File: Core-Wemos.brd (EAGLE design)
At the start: 86.5 x 100 mm, 51 parts, among them J2 CONNECTOR-GROVE-4P-2.0-347013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, J3 IO4

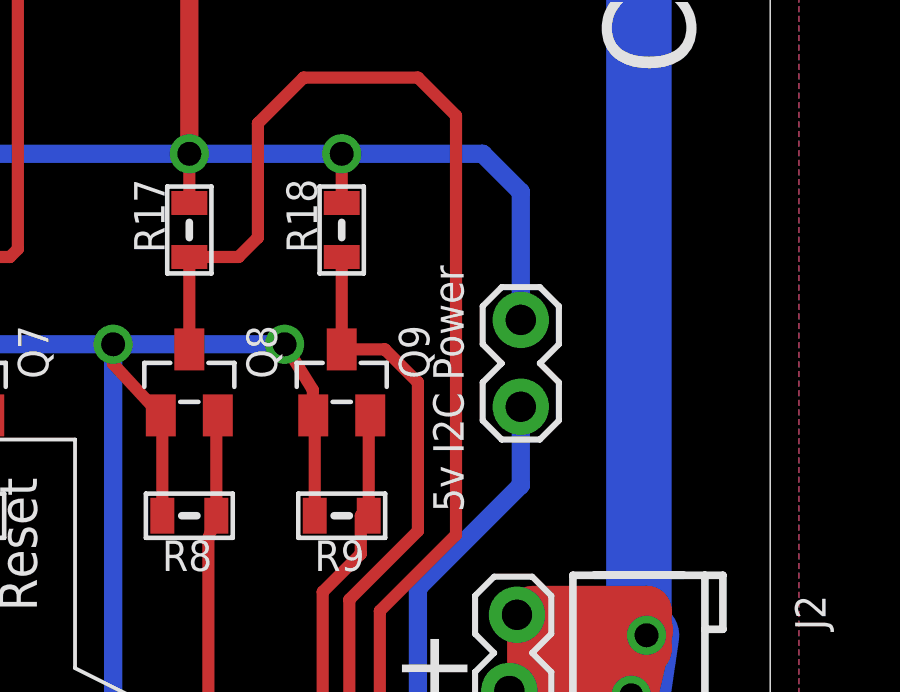
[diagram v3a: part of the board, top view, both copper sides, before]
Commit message: added missing component values
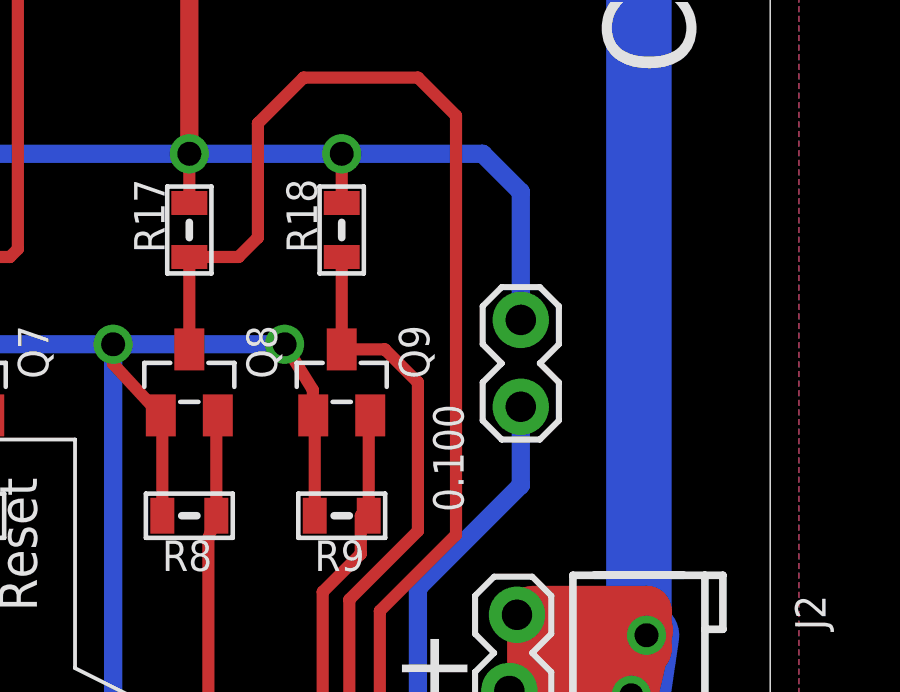
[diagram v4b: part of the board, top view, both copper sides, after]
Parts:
- CMRI-IO: value (none) -> 0.100; device SPCoast:CON-CMRI-IO -> SPCoast:1X05-CMRI-IO
- I2C-OLED: value (none) -> OLED
- JP1: value 5v I2C Power -> 0.100
- Q1, Q2, Q3, Q4, Q5, Q6, Q7, Q8, Q9: value (none) -> BSS138
- VR5.0: value 5v -> cj7805
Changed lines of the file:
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@@
 <attribute name="VALUE" x="66.04" y="74.295" size="1.27" layer="27" font="vector" rot="R180"/>
 </element>
-<element name="JP1" library="SparkFun-Connectors" package="1X02_LOCK" value="5v I2C Power" x="72.009" y="48.895" smashed="yes" rot="R90">
+<element name="JP1" library="SparkFun-Connectors" package="1X02_LOCK" value="0.100" x="72.009" y="48.895" smashed="yes" rot="R90">
 <attribute name="VALUE" x="70.104" y="45.212" size="1.016" layer="21" rot="R90"/>
 </element>
@@
 <attribute name="VALUE" x="16.79575" y="62.4205" size="1.016" layer="27" rot="R90"/>
 </element>
-<element name="VR5.0" library="SPCoast" package="TO-252" value="5v" x="20.32" y="73.66" smashed="yes" rot="R90">
+<element name="VR5.0" library="SPCoast" package="TO-252" value="cj7805" x="20.32" y="73.66" smashed="yes" rot="R90">
 <attribute name="NAME" x="21.43125" y="75.40625" size="1.016" layer="25" ratio="11" rot="R270"/>
 <attribute name="VALUE" x="21.7805" y="69.723" size="1.27" layer="27" ratio="10" rot="R180"/>
@@
 <attribute name="VALUE" x="5.08" y="67.31" size="1.27" layer="27"/>
 </element>
-<element name="Q7" library="SPCoast" package="SOT23" value="" x="53.34" y="49.53" smashed="yes" rot="R270">
+<element name="Q7" library="SPCoast" package="SOT23" value="BSS138" x="53.34" y="49.53" smashed="yes" rot="R270">
 <attribute name="NAME" x="55.245" y="51.435" size="1.016" layer="25" rot="R270"/>
 <attribute name="VALUE" x="50.165" y="51.435" size="1.27" layer="27" rot="R270"/>
@@
 <attribute name="VALUE" x="54.737" y="53.594" size="0.4064" layer="27" rot="R90"/>
 </element>
-<element name="Q8" library="SPCoast" package="SOT23" value="" x="60.96" y="49.53" smashed="yes" rot="R270">
+<element name="Q8" library="SPCoast" package="SOT23" value="BSS138" x="60.96" y="49.53" smashed="yes" rot="R270">
 <attribute name="NAME" x="62.865" y="51.435" size="1.016" layer="25" rot="R270"/>
 <attribute name="VALUE" x="57.785" y="51.435" size="1.27" layer="27" rot="R270"/>
@@
 <attribute name="VALUE" x="62.357" y="53.594" size="0.4064" layer="27" rot="R90"/>
 </element>
-<element name="Q9" library="SPCoast" package="SOT23" value="" x="66.04" y="49.53" smashed="yes" rot="R270">
+<element name="Q9" library="SPCoast" package="SOT23" value="BSS138" x="66.04" y="49.53" smashed="yes" rot="R270">
 <attribute name="NAME" x="67.945" y="51.435" size="1.016" layer="25" rot="R270"/>
 <attribute name="VALUE" x="62.865" y="51.435" size="1.27" layer="27" rot="R270"/>
@@
 <attribute name="VALUE" x="67.437" y="53.594" size="0.4064" layer="27" rot="R90"/>
 </element>
-<element name="Q1" library="SPCoast" package="SOT23" value="" x="21.59" y="49.53" smashed="yes" rot="R270">
+<element name="Q1" library="SPCoast" package="SOT23" value="BSS138" x="21.59" y="49.53" smashed="yes" rot="R270">
 <attribute name="NAME" x="23.495" y="51.435" size="1.016" layer="25" rot="R270"/>
 <attribute name="VALUE" x="18.415" y="51.435" size="1.27" layer="27" rot="R270"/>
@@
 <attribute name="VALUE" x="22.987" y="53.594" size="0.4064" layer="27" rot="R90"/>
 </element>
-<element name="Q2" library="SPCoast" package="SOT23" value="" x="26.67" y="49.53" smashed="yes" rot="R270">
+<element name="Q2" library="SPCoast" package="SOT23" value="BSS138" x="26.67" y="49.53" smashed="yes" rot="R270">
 <attribute name="NAME" x="28.575" y="51.435" size="1.016" layer="25" rot="R270"/>
 <attribute name="VALUE" x="23.495" y="51.435" size="1.27" layer="27" rot="R270"/>
@@
 <attribute name="VALUE" x="28.067" y="53.594" size="0.4064" layer="27" rot="R90"/>
 </element>
-<element name="Q3" library="SPCoast" package="SOT23" value="" x="31.75" y="49.53" smashed="yes" rot="R270">
+<element name="Q3" library="SPCoast" package="SOT23" value="BSS138" x="31.75" y="49.53" smashed="yes" rot="R270">
 <attribute name="NAME" x="33.655" y="51.435" size="1.016" layer="25" rot="R270"/>
 <attribute name="VALUE" x="28.575" y="51.435" size="1.27" layer="27" rot="R270"/>
@@
 <attribute name="VALUE" x="33.147" y="53.594" size="0.4064" layer="27" rot="R90"/>
 </element>
-<element name="Q4" library="SPCoast" package="SOT23" value="" x="40.005" y="49.53" smashed="yes" rot="R270">
+<element name="Q4" library="SPCoast" package="SOT23" value="BSS138" x="40.005" y="49.53" smashed="yes" rot="R270">
 <attribute name="NAME" x="41.91" y="51.435" size="1.016" layer="25" rot="R270"/>
 <attribute name="VALUE" x="36.83" y="51.435" size="1.27" layer="27" rot="R270"/>
@@
 <attribute name="VALUE" x="41.402" y="53.594" size="0.4064" layer="27" rot="R90"/>
 </element>
-<element name="Q5" library="SPCoast" package="SOT23" value="" x="44.45" y="49.53" smashed="yes" rot="R270">
+<element name="Q5" library="SPCoast" package="SOT23" value="BSS138" x="44.45" y="49.53" smashed="yes" rot="R270">
 <attribute name="NAME" x="46.355" y="51.435" size="1.016" layer="25" rot="R270"/>
 <attribute name="VALUE" x="41.275" y="51.435" size="1.27" layer="27" rot="R270"/>
@@
 <attribute name="VALUE" x="45.847" y="53.594" size="0.4064" layer="27" rot="R90"/>
 </element>
-<element name="Q6" library="SPCoast" package="SOT23" value="" x="48.895" y="49.53" smashed="yes" rot="R270">
+<element name="Q6" library="SPCoast" package="SOT23" value="BSS138" x="48.895" y="49.53" smashed="yes" rot="R270">
 <attribute name="NAME" x="50.8" y="51.435" size="1.016" layer="25" rot="R270"/>
 <attribute name="VALUE" x="45.72" y="51.435" size="1.27" layer="27" rot="R270"/>
@@
 <attribute name="VALUE" x="50.292" y="53.594" size="0.4064" layer="27" rot="R90"/>
 </element>
-<element name="CMRI-IO" library="SPCoast" package="CON-CMRI-IO" value="" x="6.35" y="31.75" smashed="yes" rot="R90">
+<element name="CMRI-IO" library="SPCoast" package="1X05-CMRI-IO" value="0.100" x="6.35" y="31.75" smashed="yes" rot="R90">
 <attribute name="NAME" x="6.8834" y="44.3992" size="1.016" layer="25" ratio="10" rot="R90"/>
 </element>
@@
 <attribute name="NAME" x="67.056" y="94.107" size="1.016" layer="25"/>
 </element>
-<element name="I2C-OLED" library="SPCoast" package="I2C-NOOUTLINE" value="" x="19.939" y="39.497" smashed="yes" rot="R180">
+<element name="I2C-OLED" library="SPCoast" package="I2C-NOOUTLINE" value="OLED" x="19.939" y="39.497" smashed="yes" rot="R180">
 <attribute name="NAME" x="16.637" y="43.307" size="1.016" layer="25" font="vector" ratio="11"/>
 <attribute name="VALUE" x="13.081" y="39.878" size="0.635" layer="27" font="vector" ratio="10" rot="R270"/>

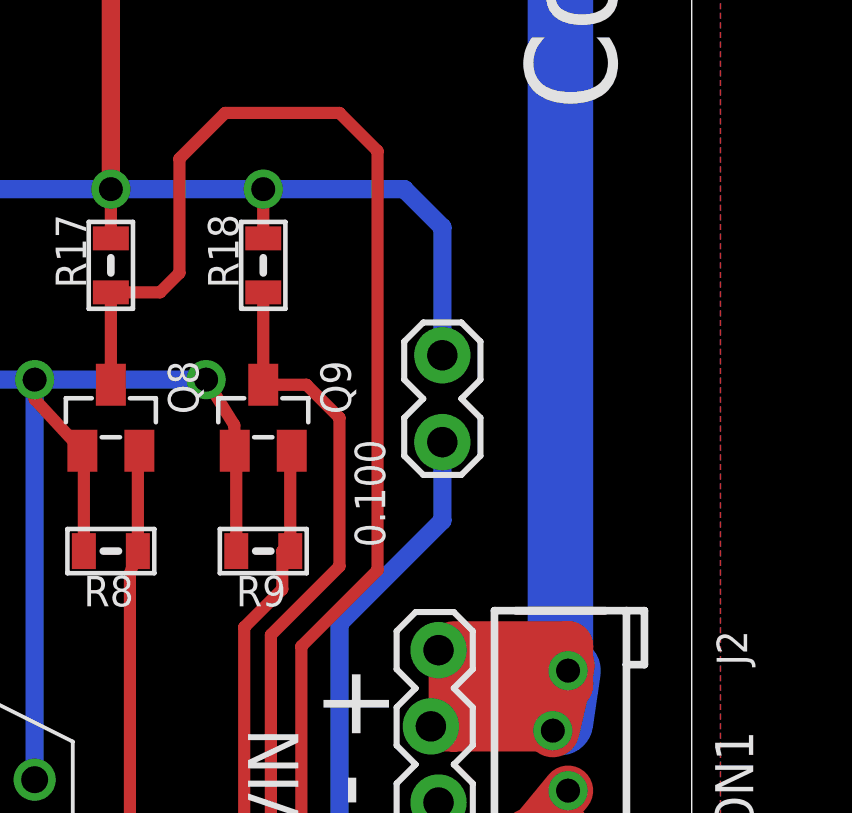
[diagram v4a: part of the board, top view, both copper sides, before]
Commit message: updated part names and values
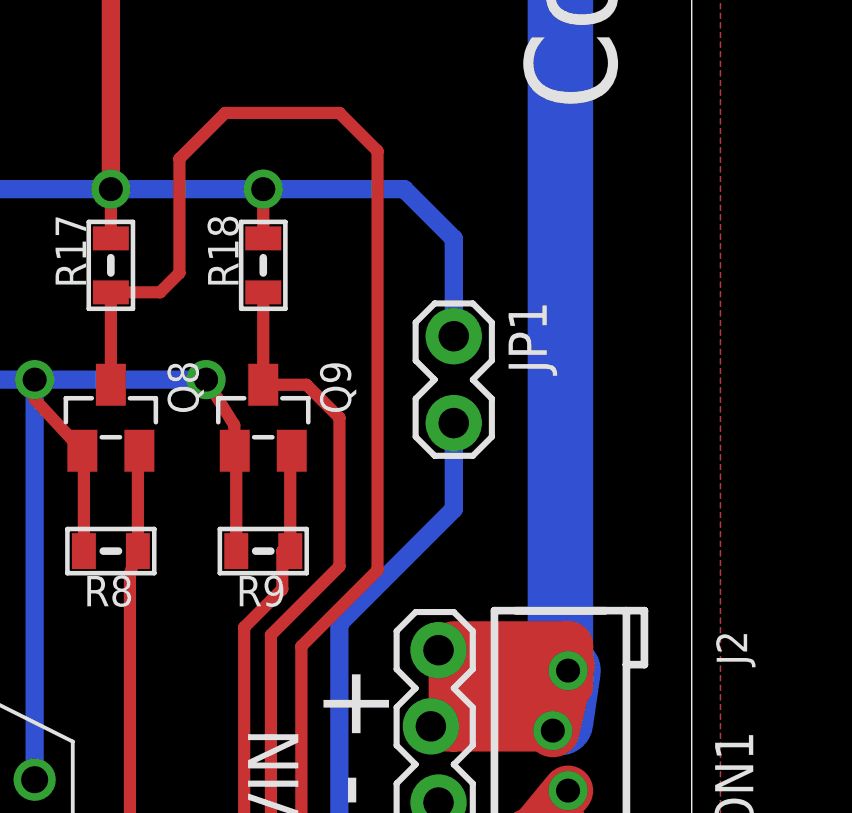
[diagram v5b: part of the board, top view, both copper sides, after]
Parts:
- removed JP2: (no value), SparkFun-Connectors:1X06_LOCK
- added IO4-6: (no value), SPCoast:1X06_LOCK
- CON1: value (none) -> 0.100
- J2: value CONNECTOR-GROVE-4P-2.0-3470130P1 -> 2mm
- JP1: value 0.100 -> (none); device SparkFun-Connectors:1X02_LOCK -> SPCoast:1X02_LOCK
- WEMOS: value D1Mini -> Mini-R2
- moved JP1 3.20 mm to (72.4, 52.1), turned to 270 degrees
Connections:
- net D3H: now also IO4-6.2; no longer JP2.2
- net D4H: now also IO4-6.3; no longer JP2.3
- net D5H: now also IO4-6.4; no longer JP2.4
- net D6H: now also IO4-6.5; no longer JP2.5
- net GND: now also IO4-6.6; no longer JP2.6
- net N$44: now also JP1.2; no longer JP1.1
- net VCCIO: now also IO4-6.1, JP1.1; no longer JP1.2, JP2.1
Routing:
- net N$44: track 36.3 -> 37.1 mm
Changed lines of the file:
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@@
 <attribute name="AMP" value="520250-3" x="58.42" y="84.963" size="1.778" layer="27" rot="R180" display="off"/>
 </element>
-<element name="JP2" library="SparkFun-Connectors" package="1X06_LOCK" value="" x="64.77" y="70.993" smashed="yes" rot="R180">
+<element name="IO4-6" library="SPCoast" package="1X06_LOCK" value="" x="64.77" y="70.993" smashed="yes" rot="R180">
 <attribute name="VALUE" x="66.04" y="74.295" size="1.27" layer="27" font="vector" rot="R180"/>
-</element>
-<element name="JP1" library="SparkFun-Connectors" package="1X02_LOCK" value="0.100" x="72.009" y="48.895" smashed="yes" rot="R90">
-<attribute name="VALUE" x="70.104" y="45.212" size="1.016" layer="21" rot="R90"/>
 </element>
 <element name="I2C" library="SPCoast" package="I2C-L" value="CONNECTOR-I2CLEFT" x="72.39" y="26.035" smashed="yes">
 <attribute name="NAME" x="76.708" y="21.971" size="1.016" layer="25" font="vector" ratio="11" rot="R90"/>
 </element>
-<element name="J2" library="SPCoast" package="4P-2.0" value="CONNECTOR-GROVE-4P-2.0-3470130P1" x="75.946" y="38.1" smashed="yes" rot="R90">
+<element name="J2" library="SPCoast" package="4P-2.0" value="2mm" x="75.946" y="38.1" smashed="yes" rot="R90">
 <attribute name="NAME" x="82.169" y="41.275" size="1.016" layer="25" font="vector" ratio="11" rot="R90"/>
 </element>
@@
 <attribute name="VALUE" x="67.46875" y="75.1205" size="1.016" layer="27" rot="R90"/>
 </element>
-<element name="WEMOS" library="SPCoast" package="WEMOS-D1" value="D1Mini" x="46.99" y="29.845" smashed="yes" rot="R180"/>
+<element name="WEMOS" library="SPCoast" package="WEMOS-D1" value="Mini-R2" x="46.99" y="29.845" smashed="yes" rot="R180"/>
 <element name="C3" library="SPCoast" package="0810-CAP" value="150uF" x="8.255" y="67.945" smashed="yes" rot="R270">
 <attribute name="NAME" x="10.2648" y="71.1406" size="1.016" layer="25"/>
@@
 <attribute name="VALUE" x="4.953" y="88.9" size="1.27" layer="27" rot="R180"/>
 </element>
-<element name="CON1" library="SPCoast" package="1X04_LOCK" value="" x="71.755" y="34.163" smashed="yes" rot="R90">
+<element name="CON1" library="SPCoast" package="1X04_LOCK" value="0.100" x="71.755" y="34.163" smashed="yes" rot="R90">
 <attribute name="NAME" x="82.3722" y="34.5948" size="1.27" layer="25" ratio="10" rot="R90"/>
 <attribute name="VALUE" x="74.93" y="32.893" size="1.27" layer="27" rot="R90"/>
 </element>
+<element name="JP1" library="SPCoast" package="1X02_LOCK" value="" x="72.39" y="52.07" rot="R270"/>
 </elements>
 <signals>
@@
 </polygon>
 <contactref element="J3" pad="6"/>
-<contactref element="JP2" pad="6"/>
+<contactref element="IO4-6" pad="6"/>
 <via x="25.4" y="72.39" extent="1-16" drill="0.8"/>
 <via x="25.4" y="76.2" extent="1-16" drill="0.8"/>
@@
 <signal name="VCCIO" class="1">
 <contactref element="J3" pad="1"/>
-<contactref element="JP2" pad="1"/>
-<contactref element="JP1" pad="2"/>
+<contactref element="IO4-6" pad="1"/>
 <contactref element="C4" pad="1"/>
 <contactref element="WEMOS" pad="5V"/>
@@
 <wire x1="53.34" y1="57.15" x2="60.96" y2="57.15" width="0.6096" layer="16"/>
 <wire x1="66.04" y1="57.15" x2="70.739" y2="57.15" width="0.6096" layer="16"/>
-<wire x1="70.739" y1="57.15" x2="72.009" y2="55.88" width="0.6096" layer="16"/>
-<wire x1="72.009" y1="55.88" x2="72.009" y2="51.6128" width="0.6096" layer="16"/>
+<wire x1="70.739" y1="57.15" x2="72.39" y2="55.499" width="0.6096" layer="16"/>
 <wire x1="64.77" y1="70.993" x2="64.77" y2="72.898" width="0.4064" layer="1"/>
 <wire x1="64.77" y1="72.898" x2="63.1825" y2="74.4855" width="0.4064" layer="1"/>
@@
 <wire x1="22.606" y1="66.04" x2="22.606" y2="64.781" width="0.8128" layer="1"/>
 <wire x1="24.13" y1="66.04" x2="22.606" y2="66.04" width="0.8128" layer="1"/>
+<contactref element="JP1" pad="1"/>
+<wire x1="72.39" y1="55.499" x2="72.39" y2="52.2478" width="0.6096" layer="16"/>
 </signal>
 <signal name="N$44">
-<contactref element="JP1" pad="1"/>
 <contactref element="I2C" pad="V+"/>
 <contactref element="I2C" pad="V+@1"/>
@@
 <wire x1="74.676" y1="19.177" x2="73.899" y2="18.4" width="0.4064" layer="16"/>
 <wire x1="73.899" y1="18.4" x2="72.136" y2="18.4" width="0.4064" layer="16"/>
-<wire x1="72.009" y1="48.7172" x2="72.009" y2="46.101" width="0.6096" layer="16"/>
-<wire x1="72.009" y1="46.101" x2="68.58" y2="42.672" width="0.6096" layer="16"/>
+<wire x1="72.39" y1="46.482" x2="68.58" y2="42.672" width="0.6096" layer="16"/>
 <wire x1="68.58" y1="42.672" x2="68.58" y2="33.02" width="0.6096" layer="16"/>
 <wire x1="68.58" y1="33.02" x2="72.009" y2="29.591" width="0.6096" layer="16"/>
 <wire x1="72.009" y1="29.591" x2="72.009" y2="27.813" width="0.6096" layer="16"/>
 <wire x1="72.009" y1="27.813" x2="73.66" y2="26.162" width="0.6096" layer="16"/>
+<contactref element="JP1" pad="2"/>
+<wire x1="72.39" y1="46.482" x2="72.39" y2="49.3522" width="0.6096" layer="16"/>
 </signal>
 <signal name="D3H" class="2">
@@
 <wire x1="54.98" y1="53.71" x2="55.245" y2="53.975" width="0.4064" layer="1"/>
 <contactref element="J3" pad="2"/>
-<contactref element="JP2" pad="2"/>
+<contactref element="IO4-6" pad="2"/>
 <wire x1="60.325" y1="78.613" x2="60.325" y2="72.898" width="0.254" layer="16"/>
 <wire x1="60.325" y1="72.898" x2="62.23" y2="71.247" width="0.4064" layer="16"/>
@@
 <wire x1="50.8" y1="53.975" x2="50.8" y2="62.103" width="0.4064" layer="1"/>
 <contactref element="J3" pad="3"/>
-<contactref element="JP2" pad="3"/>
+<contactref element="IO4-6" pad="3"/>
 <wire x1="59.055" y1="76.073" x2="59.055" y2="71.628" width="0.254" layer="16"/>
 <wire x1="59.055" y1="71.628" x2="59.69" y2="70.993" width="0.4064" layer="16"/>
@@
 <wire x1="46.355" y1="53.975" x2="46.355" y2="60.452" width="0.4064" layer="1"/>
 <contactref element="J3" pad="4"/>
-<contactref element="JP2" pad="4"/>
+<contactref element="IO4-6" pad="4"/>
 <wire x1="57.785" y1="78.613" x2="57.785" y2="71.628" width="0.254" layer="16"/>
 <wire x1="57.785" y1="71.628" x2="57.15" y2="71.247" width="0.4064" layer="16"/>
@@
 <wire x1="41.91" y1="53.975" x2="41.91" y2="58.293" width="0.4064" layer="1"/>
 <contactref element="J3" pad="5"/>
-<contactref element="JP2" pad="5"/>
+<contactref element="IO4-6" pad="5"/>
 <wire x1="56.515" y1="76.073" x2="56.515" y2="72.898" width="0.254" layer="16"/>
 <wire x1="56.515" y1="72.898" x2="54.61" y2="70.993" width="0.4064" layer="16"/>

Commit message: FIDs
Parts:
- removed FID-LL, FID-UR: FIDUCIAL, SPCoast:FIDUCIAL_1MM
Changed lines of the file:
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@@
 IO4 breakout, and
 I2C master</text>
-<text x="73.8472" y="53.467" size="3.81" layer="52" font="vector" ratio="15" rot="MR0">Core WeMOS
+<text x="70.0372" y="59.817" size="3.81" layer="52" font="vector" ratio="15" rot="MR0">Core WeMOS
 D1 Mini</text>
 <text x="77.2521" y="24.7087" size="1.778" layer="52" font="vector" rot="MR90">Model Railroading is fun!</text>
@@
 <attribute name="NAME" x="66.421" y="3.937" size="1.016" layer="25"/>
 </element>
-<element name="FID-LL" library="SPCoast" package="FIDUCIAL_1MM" value="FIDUCIAL" x="9.652" y="5.715" smashed="yes">
-<attribute name="NAME" x="9.017" y="3.175" size="1.016" layer="25"/>
-</element>
-<element name="FID-UR" library="SPCoast" package="FIDUCIAL_1MM" value="FIDUCIAL" x="70.231" y="92.837" smashed="yes">
-<attribute name="NAME" x="67.056" y="94.107" size="1.016" layer="25"/>
-</element>
 <element name="I2C-OLED" library="SPCoast" package="I2C-NOOUTLINE" value="OLED" x="19.939" y="39.497" smashed="yes" rot="R180">

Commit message: updated part names
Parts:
- BOARD: value BOARD80X150 -> BOARD80X80
- IO4-6, JP1: value (none) -> 0.100
- J1: value (none) -> 2.1mm
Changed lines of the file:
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@@
 <attribute name="AMP" value="520250-3" x="58.42" y="84.963" size="1.778" layer="27" rot="R180" display="off"/>
 </element>
-<element name="IO4-6" library="SPCoast" package="1X06_LOCK" value="" x="64.77" y="70.993" smashed="yes" rot="R180">
+<element name="IO4-6" library="SPCoast" package="1X06_LOCK" value="0.100" x="64.77" y="70.993" smashed="yes" rot="R180">
 <attribute name="VALUE" x="66.04" y="74.295" size="1.27" layer="27" font="vector" rot="R180"/>
 </element>
@@
 <attribute name="NAME" x="82.169" y="41.275" size="1.016" layer="25" font="vector" ratio="11" rot="R90"/>
 </element>
-<element name="J1" library="SPCoast" package="DCJ0202" value="" x="13.97" y="24.13" smashed="yes"/>
+<element name="J1" library="SPCoast" package="DCJ0202" value="2.1mm" x="13.97" y="24.13" smashed="yes"/>
 <element name="LABEL1" library="SPCoast" package="PWR_LABEL" value="7-12vDC" x="25.4" y="15.24" smashed="yes" rot="R90">
 <attribute name="VALUE" x="28.575" y="13.97" size="1.27" layer="21" rot="R180"/>
 </element>
-<element name="BOARD" library="SPCoast" package="BOARD-DINRAIL-3.17INX8CM-NOHOLES" value="BOARD80X150" x="0" y="0" smashed="yes"/>
+<element name="BOARD" library="SPCoast" package="BOARD-DINRAIL-3.17INX8CM-NOHOLES" value="BOARD80X80" x="0" y="0" smashed="yes"/>
 <element name="C2" library="SPCoast" package="0805-CAP" value="10uF" x="22.606" y="63.881" smashed="yes" rot="R270">
 <attribute name="NAME" x="22.30935625" y="61.964490625" size="1.016" layer="25" rot="R270"/>
@@
 <attribute name="VALUE" x="74.93" y="32.893" size="1.27" layer="27" rot="R90"/>
 </element>
-<element name="JP1" library="SPCoast" package="1X02_LOCK" value="" x="72.39" y="52.07" rot="R270"/>
+<element name="JP1" library="SPCoast" package="1X02_LOCK" value="0.100" x="72.39" y="52.07" rot="R270"/>
 </elements>
 <signals>
